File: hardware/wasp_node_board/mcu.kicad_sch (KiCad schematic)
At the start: 35 parts, among them J3 Conn_02x10_Odd_Even, J6 TC2030, SW2 C&K KMR231NG LFS, U1 STM32H723ZGTx, U3 APS6404L-3SQRx-SN, Y2 ASE-25.000MHZ-L-K-T

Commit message: Removed some stuff and got the general placement down
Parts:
- removed J3: Conn_02x10_Odd_Even, Connector_PinHeader_2.54mm:PinHeader_2x10_P2.54mm_Vertical, symbol Connector_Generic:Conn_02x10_Odd_Even

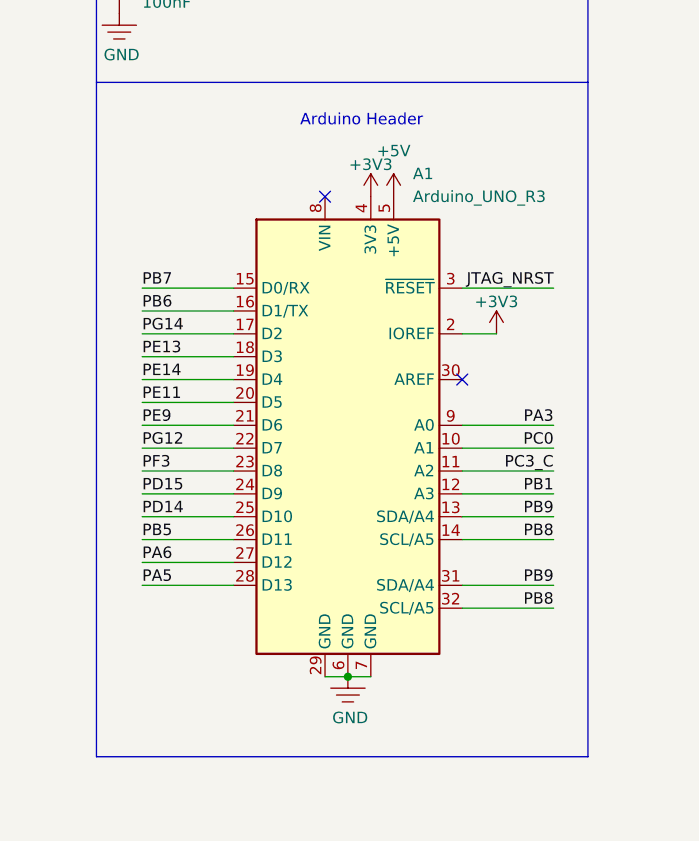
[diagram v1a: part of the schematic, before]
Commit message: Layout candidate done. Now to add back some functionality
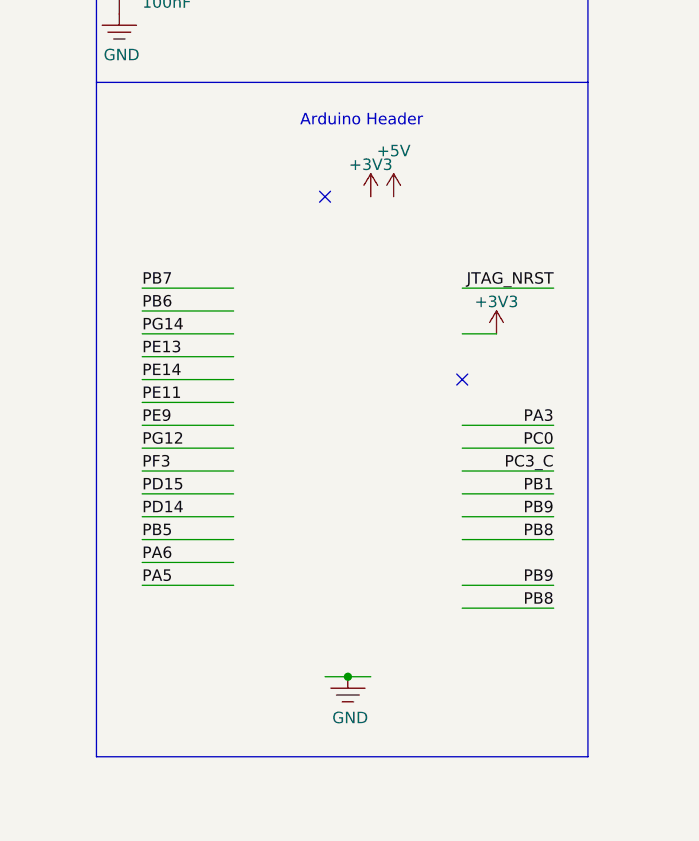
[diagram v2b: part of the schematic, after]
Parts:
- removed A1: Arduino_UNO_R3, Arduino_UNO_R3_Headers:Arduino_UNO_R3_Headers, symbol MCU_Module:Arduino_UNO_R3

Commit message: V1 layout done
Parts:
- added D4: LTST-C191KSKT, LED_SMD:LED_0603_1608Metric, symbol Device:LED
- added J8, J9: Conn_02x05_Odd_Even, Connector_PinHeader_2.54mm:PinHeader_2x05_P2.54mm_Vertical_SMD, symbol Connector_Generic:Conn_02x05_Odd_Even
- added R28: 1k, Resistor_SMD:R_0402_1005Metric, symbol Device:R_Small
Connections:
- net +3V3: now also J8.1 (Pin_1), J9.1 (Pin_1)
- net GND: now also J8.10 (Pin_10), J8.2 (Pin_2), J9.10 (Pin_10), J9.2 (Pin_2), R28.1
- net I2C2_SCL: now also J8.5 (Pin_5)
- net I2C2_SDA: now also J8.6 (Pin_6)
- net PA0: now also J8.7 (Pin_7)
- net PA8: now also J9.9 (Pin_9)
- net PB5: now also J8.9 (Pin_9)
- net PE9: now also J8.8 (Pin_8)
- net SPI2_CS: now also J9.8 (Pin_8)
- net SPI2_MISO: now also J9.6 (Pin_6)
- net SPI2_MOSI: now also J9.7 (Pin_7)
- net SPI2_SCK: now also J9.5 (Pin_5)
- net USART3_RX: now also J9.4 (Pin_4)
- net USART3_TX: now also J9.3 (Pin_3)
- net status_led: now reaches U1.46 (PB0)
- net status_led: now also D4.2 (A)
- net PB6 renamed LPUART1_TX
- net LPUART1_TX: now also J8.3 (Pin_3)
- net PB7 renamed LPUART1_RX
- net LPUART1_RX: now also J8.4 (Pin_4)
- new net: D4.1 (K), R28.2
- no-connect marks 56 -> 53
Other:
- note removed: "Arduino Header"
